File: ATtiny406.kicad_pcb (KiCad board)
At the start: 2 copper layers, 35.6 x 21.6 mm, 17 parts, among them J1 Conn_01x06_Male, J2 Conn_01x10_Male, J3 Conn_01x10_Male, SW1 SW_Push, U1 ATtiny406-S

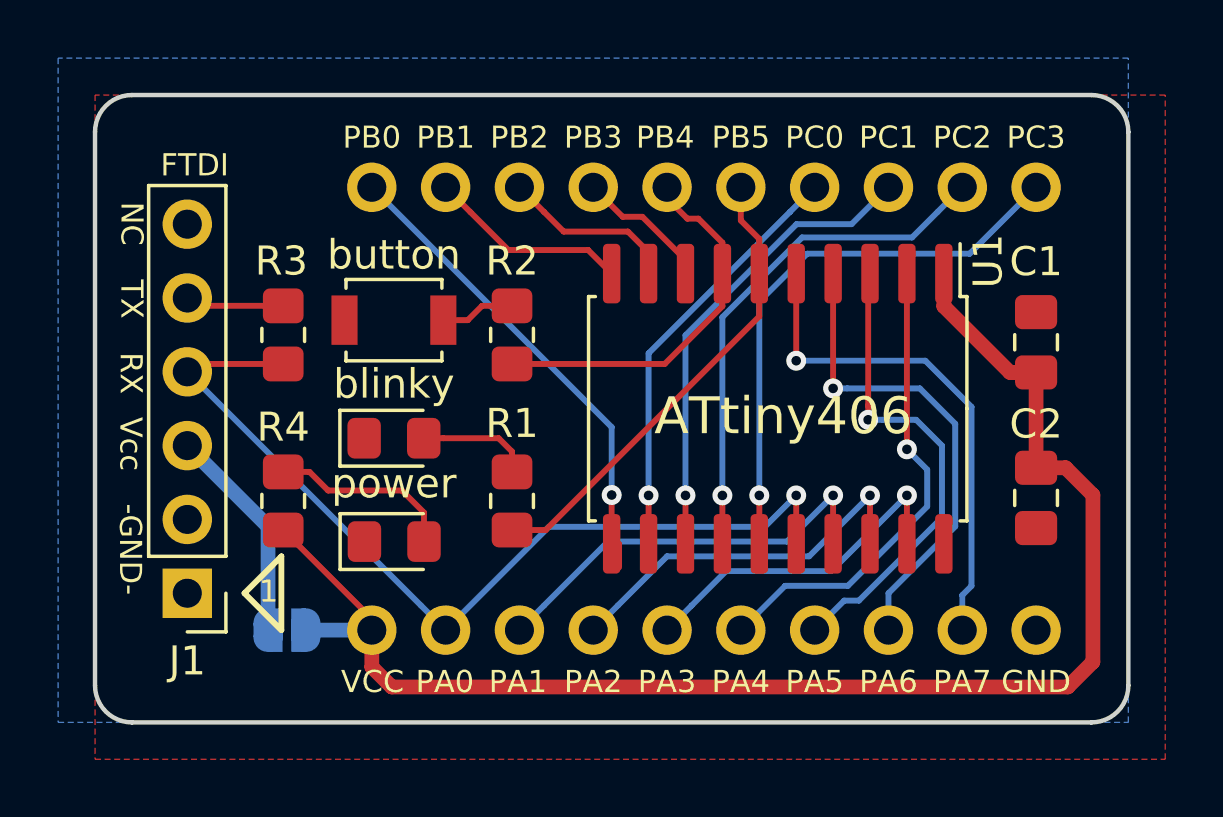
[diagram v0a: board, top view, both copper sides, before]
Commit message: Revision 1 Release
Revision 1 changes: Changed PA0 from J1 pin 4 to pin 5.
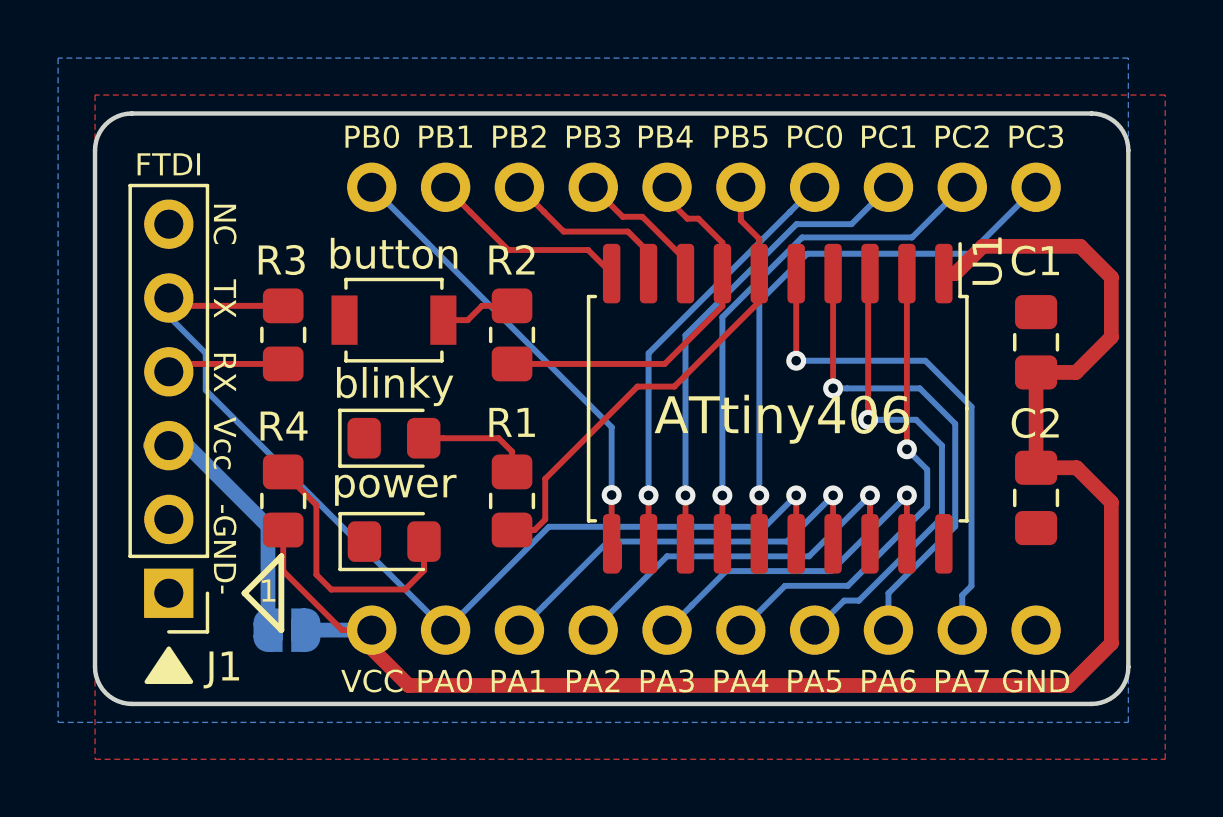
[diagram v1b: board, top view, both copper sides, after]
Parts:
- moved G*** 0.63 mm to (153.0, 83.8)
- moved J1 0.63 mm to (144.1, 90.2)
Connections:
- J1 pad 4: /PA0 -> /RX
- J1 pad 5: /TX -> /PA0
- R3 pad 1: /PA0 -> /RX
- R3 pad 2: /TX -> /PA0
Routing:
- net VCC: track 50.3 -> 57.8 mm
- net /RX: track 0.00 -> 4.68 mm
- net /PA0: track 31.7 -> 36.0 mm
- net /TX: track 3.41 -> 0.00 mm
- net Net-(D2-Pad2): track 6.42 -> 9.19 mm
- net Net-(J1-Pad3): track 7.50 -> 8.77 mm
- net /PB5: track 16.3 -> 16.8 mm
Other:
- board size 35.6 x 21.6 mm -> 35.6 x 20.3 mm
- board text added: "P/N: AT406BRD, Rev. 1 S/N:"
- board text removed: "DC Electronics"
- board text removed: "P/N: AT406BRD, Rev. 0 S/N:"
